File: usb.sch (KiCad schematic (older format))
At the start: 17 parts, among them J4 CONN_02X03, U1 LFE5U-85F-6BG381C, Y1 FNETHE025

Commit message: better RGB-OUT
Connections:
- net FTDI_RXD is gone; now on net LTDC_FROM_FPGA_G6: U1.L4 (PL56C)
- net LTDC_FROM_FPGA_B4 is gone; now on net LTDC_FROM_FPGA_G7: U1.L1 (PL65C)
- net LTDC_FROM_FPGA_R3 is gone; now on net LTDC_FROM_FPGA_R4: U1.G1 (PCLKC6_0)
- net OLED_CLK is gone; now on net LTDC_FROM_FPGA_B6: U1.P4 (GPLL0C_IN)
- net OLED_RES is gone; now on net LTDC_FROM_FPGA_B3: U1.P2 (PL92B)
- net WIFI_GPIO21 is gone; now on net LTDC_FROM_FPGA_G3: U1.K5 (VREF1_6)
- net LTDC_FROM_FPGA_B3: no longer U1.N3 (PL86A)
- net LTDC_FROM_FPGA_B6: no longer U1.N2 (PL65A)
- net LTDC_FROM_FPGA_DE: no longer U1.N5 (PL83B)
- net LTDC_FROM_FPGA_G3: no longer U1.H1 (PL53C)
- net LTDC_FROM_FPGA_G4: now also U1.K4 (PL56A); no longer U1.K2 (PL53A)
- net LTDC_FROM_FPGA_G6: no longer U1.K4 (PL56A)
- net LTDC_FROM_FPGA_G7: no longer U1.N4 (PL83C)
- net LTDC_FROM_FPGA_R4: no longer U1.J5 (PL50B)
- net LTDC_FROM_FPGA_R6: now also U1.H1 (PL53C); no longer U1.J1 (PL53B)
- net LTDC_FROM_FPGA_R7: now also U1.J5 (PL50B); no longer U1.K1 (PL53D)
- net FTDI_TXDEN renamed LTDC_FROM_FPGA_G2
- net LTDC_FROM_FPGA_B7 renamed OLED_DC
- net WIFI_RXD renamed LTDC_FROM_FPGA_G5
- new net OLED_CS: U1.N2 (PL65A)
- new net SD_CD: U1.N5 (PL83B)
- new net SD_CMD: U1.J1 (PL53B)
- new net SD_D2: U1.K1 (PL53D)
- new net SD_D3: U1.K2 (PL53A)
- new net WIFI_GPIO19: U1.N4 (PL83C)
- new net WIFI_GPIO27: U1.N3 (PL86A)
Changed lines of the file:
@@
 Text GLabel 10150 2650 2    60   Input ~ 0
 FTDI_TXD
-Text GLabel 8650 1950 0    60   Input ~ 0
-FTDI_RXD
 Text GLabel 10150 2450 2    60   Input ~ 0
 FTDI_nRTS
 Text GLabel 10150 2550 2    60   Input ~ 0
 FTDI_nDTR
-Text GLabel 8650 2050 0    60   Input ~ 0
-WIFI_TXD
-Text GLabel 10150 1550 2    60   Input ~ 0
-WIFI_RXD
 Text GLabel 10150 2350 2    60   Input ~ 0
 WIFI_GPIO0
 Text GLabel 10150 1450 2    60   Input ~ 0
 WIFI_EN
-Text GLabel 10150 2850 2    60   Input ~ 0
-OLED_RES
-Text GLabel 8650 2750 0    60   Input ~ 0
-OLED_MOSI
-Text GLabel 10150 2750 2    60   Input ~ 0
-OLED_CLK
 Text GLabel 8650 2850 0    60   Input ~ 0
 OLED_DC
@@
 Connection ~ 2600 2850
 Connection ~ 2700 2750
-Text GLabel 8650 2550 0    60   Input ~ 0
-WIFI_GPIO26
-Wire Wire Line
-	10150 1350 10750 1350
-Text Label 10200 1350 0    60   ~ 0
-ANT_433MHz
 Text Notes 650  4100 0    60   ~ 0
 D8,D9: Schottky 2A/30V \nLow drop Vfmax=0.375V\nParts reduction: Only D8 is required.\nD9 D51 D52 can be 1206\n1A polyfuses or 0-ohm/2A jumpers
@@
 Text Notes 2750 5350 0    60   ~ 0
 D- 1.5k pullp for \nlow speed device\nmode USB1.0
-Text GLabel 8650 2350 0    60   Input ~ 0
-FTDI_TXDEN
 $Comp
 L lfe5bg381:LFE5UM-85F-6BG381C U1
@@
 Text Label 1850 2650 0    60   ~ 0
 US2VBUS
-Text GLabel 8650 1750 0    60   Input ~ 0
-SD_D1
 Text Notes 750  6050 0    60   ~ 0
 Deviation from USB specification in\npulldowns for BOM simplificaton.\nWith series diode, correct value R63 R64 \nshould be 12k but 15k is used.
@@
 Text GLabel 10150 1950 2    60   Input ~ 0
 FTDI_nRXLED
-Text GLabel 10150 2050 2    60   Input ~ 0
-WIFI_GPIO21
-Text GLabel 10150 1650 2    60   Input ~ 0
-WIFI_GPIO22
 Text GLabel 8650 1650 0    60   Input ~ 0
 OLED_BL
-Text GLabel 7050 2450 0    60   Input ~ 0
+Text GLabel 10150 2850 2    60   Input ~ 0
 LTDC_FROM_FPGA_B3
-Text GLabel 7050 2550 0    60   Input ~ 0
-LTDC_FROM_FPGA_B4
-Text GLabel 7050 2650 0    60   Input ~ 0
+Text GLabel 10150 2750 2    60   Input ~ 0
 LTDC_FROM_FPGA_B6
-Text GLabel 11800 1750 2    60   Input ~ 0
-LTDC_FROM_FPGA_R7
-Text GLabel 11800 1650 2    60   Input ~ 0
+Text GLabel 10200 1350 2    60   Input ~ 0
 LTDC_FROM_FPGA_R4
-Text GLabel 11800 1950 2    60   Input ~ 0
-LTDC_FROM_FPGA_R5
-Text GLabel 11800 1850 2    60   Input ~ 0
+Text GLabel 8650 1750 0    60   Input ~ 0
 LTDC_FROM_FPGA_R6
-Text GLabel 7050 1650 0    60   Input ~ 0
+Text GLabel 6200 1650 0    60   Input ~ 0
 LTDC_FROM_FPGA_CLK
 Text GLabel 11800 2250 2    60   Input ~ 0
 LTDC_FROM_FPGA_DE
-Text GLabel 7050 2150 0    60   Input ~ 0
+Text GLabel 8650 2550 0    60   Input ~ 0
 LTDC_FROM_FPGA_G7
-Text GLabel 7050 2050 0    60   Input ~ 0
+Text GLabel 8650 1950 0    60   Input ~ 0
 LTDC_FROM_FPGA_G6
-Text GLabel 7050 1950 0    60   Input ~ 0
+Text GLabel 10150 1550 2    60   Input ~ 0
 LTDC_FROM_FPGA_G5
-Text GLabel 7050 1850 0    60   Input ~ 0
+Text GLabel 10150 2050 2    60   Input ~ 0
+LTDC_FROM_FPGA_G3
+Text GLabel 8650 2350 0    60   Input ~ 0
+LTDC_FROM_FPGA_G2
+Text GLabel 6300 1650 2    60   Input ~ 0
+OLED_BL
+Wire Wire Line
+	6200 1650 6300 1650
+Text GLabel 8650 2750 0    60   Input ~ 0
+LTDC_FROM_FPGA_B5
+Wire Wire Line
+	10150 1350 10200 1350
+Text GLabel 8650 2050 0    60   Input ~ 0
 LTDC_FROM_FPGA_G4
-Text GLabel 7050 1750 0    60   Input ~ 0
-LTDC_FROM_FPGA_G3
-Text GLabel 7050 2350 0    60   Input ~ 0
-LTDC_FROM_FPGA_G2
-Text GLabel 7150 1650 2    60   Input ~ 0
-OLED_BL
-Text GLabel 7150 1750 2    60   Input ~ 0
-SD_D1
-Text GLabel 7150 1850 2    60   Input ~ 0
-SD_D3
-Text GLabel 7150 1950 2    60   Input ~ 0
-FTDI_RXD
-Text GLabel 7150 2050 2    60   Input ~ 0
-WIFI_TXD
-Text GLabel 7150 2150 2    60   Input ~ 0
-WIFI_GPIO19
-Text GLabel 7150 2350 2    60   Input ~ 0
-FTDI_TXDEN
-Text GLabel 7150 2450 2    60   Input ~ 0
-WIFI_GPIO27
-Text GLabel 7150 2550 2    60   Input ~ 0
-WIFI_GPIO26
-Text GLabel 7150 2650 2    60   Input ~ 0
-OLED_CS
-Text GLabel 7150 2750 2    60   Input ~ 0
-OLED_MOSI
-Text GLabel 7150 2850 2    60   Input ~ 0
-OLED_DC
-Wire Wire Line
-	7050 1650 7150 1650
-Wire Wire Line
-	7050 1750 7150 1750
-Wire Wire Line
-	7050 1850 7150 1850
-Wire Wire Line
-	7050 1950 7150 1950
-Wire Wire Line
-	7050 2050 7150 2050
-Wire Wire Line
-	7050 2150 7150 2150
-Wire Wire Line
-	7050 2350 7150 2350
-Wire Wire Line
-	7050 2450 7150 2450
-Wire Wire Line
-	7150 2550 7050 2550
-Wire Wire Line
-	7050 2650 7150 2650
-Wire Wire Line
-	7050 2750 7150 2750
-Wire Wire Line
-	7150 2850 7050 2850
-Text GLabel 11700 1650 0    60   Input ~ 0
-WIFI_GPIO22
-Text GLabel 11700 1750 0    60   Input ~ 0
-SD_D2
-Text GLabel 11700 1850 0    60   Input ~ 0
-SD_CMD
-Text GLabel 11700 1950 0    60   Input ~ 0
-FTDI_nRXLED
-Text GLabel 11700 2250 0    60   Input ~ 0
-SD_CD
-Wire Wire Line
-	11800 1650 11700 1650
-Wire Wire Line
-	11700 1750 11800 1750
-Wire Wire Line
-	11800 1850 11700 1850
-Wire Wire Line
-	11700 1950 11800 1950
-Wire Wire Line
-	11700 2250 11800 2250
-Text GLabel 10750 1350 2    60   Input ~ 0
-LTDC_FROM_FPGA_R3
-Text GLabel 7050 2750 0    60   Input ~ 0
-LTDC_FROM_FPGA_B5
-Text GLabel 7050 2850 0    60   Input ~ 0
-LTDC_FROM_FPGA_B7
+Text GLabel 10150 1650 2    60   Input ~ 0
+LTDC_FROM_FPGA_R7
 $EndSCHEMATC

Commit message: More fixes
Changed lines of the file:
@@
 Text GLabel 10150 1950 2    60   Input ~ 0
 FTDI_nRXLED
-Text GLabel 8650 1650 0    60   Input ~ 0
-OLED_BL
 Text GLabel 10150 2850 2    60   Input ~ 0
 LTDC_FROM_FPGA_B3
@@
 Text GLabel 8650 1750 0    60   Input ~ 0
 LTDC_FROM_FPGA_R6
-Text GLabel 6200 1650 0    60   Input ~ 0
+Text GLabel 8650 1650 0    60   Input ~ 0
 LTDC_FROM_FPGA_CLK
 Text GLabel 11800 2250 2    60   Input ~ 0
@@
 Text GLabel 8650 2350 0    60   Input ~ 0
 LTDC_FROM_FPGA_G2
-Text GLabel 6300 1650 2    60   Input ~ 0
-OLED_BL
-Wire Wire Line
-	6200 1650 6300 1650
 Text GLabel 8650 2750 0    60   Input ~ 0
 LTDC_FROM_FPGA_B5

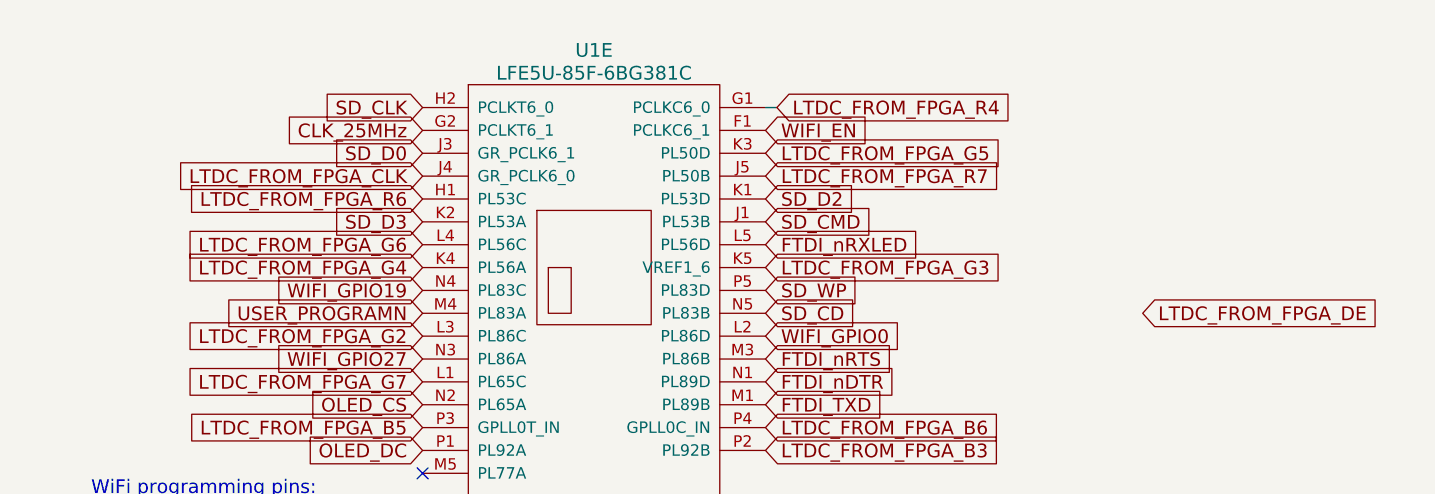
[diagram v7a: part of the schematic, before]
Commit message: Adding all SPI to FPGA resorting LCD TO FPGA
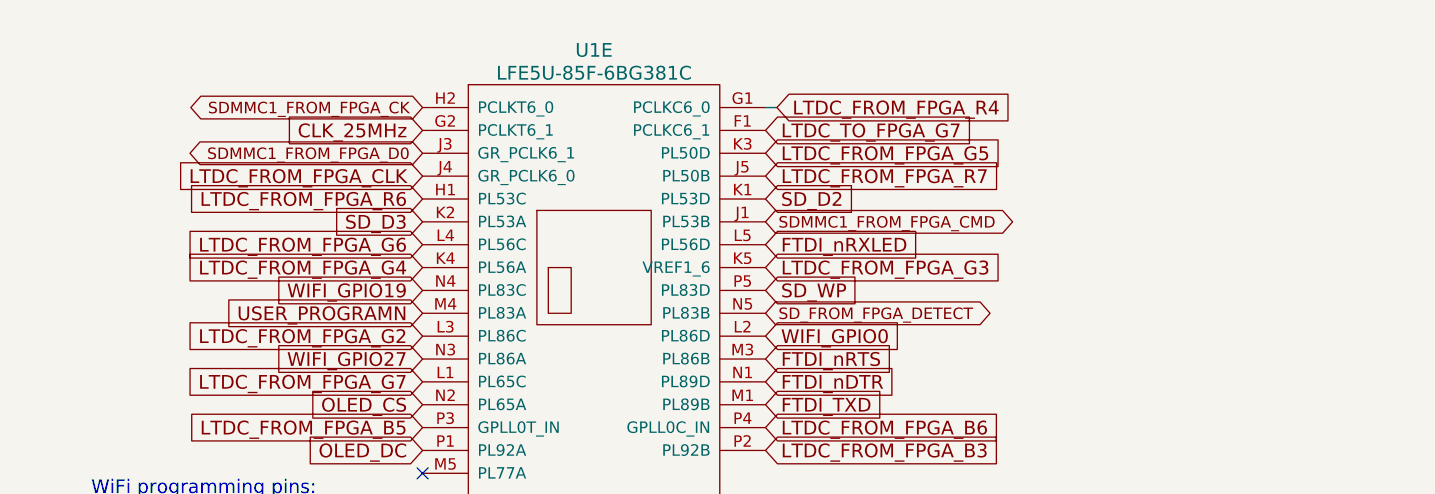
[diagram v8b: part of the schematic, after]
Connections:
- net SD_CD renamed SD_FROM_FPGA_DETECT
- net SD_CLK renamed SDMMC1_FROM_FPGA_CK
- net SD_CMD renamed SDMMC1_FROM_FPGA_CMD
- net SD_D0 renamed SDMMC1_FROM_FPGA_D0
- net WIFI_EN renamed LTDC_TO_FPGA_G7
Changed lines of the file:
@@
 Text GLabel 10150 2350 2    60   Input ~ 0
 WIFI_GPIO0
-Text GLabel 10150 1450 2    60   Input ~ 0
-WIFI_EN
 Text GLabel 8650 2850 0    60   Input ~ 0
 OLED_DC
 Text GLabel 8650 2650 0    60   Input ~ 0
 OLED_CS
-Text GLabel 8650 1550 0    60   Input ~ 0
-SD_D0
 Text GLabel 10150 1750 2    60   Input ~ 0
 SD_D2
 Text GLabel 8650 1850 0    60   Input ~ 0
 SD_D3
-Text GLabel 8650 1350 0    60   Input ~ 0
-SD_CLK
-Text GLabel 10150 1850 2    60   Input ~ 0
-SD_CMD
 Text GLabel 10150 2150 2    60   Input ~ 0
 SD_WP
-Text GLabel 10150 2250 2    60   Input ~ 0
-SD_CD
 Text Notes 7200 3150 0    60   ~ 0
 WiFi programming pins:\nTXD RXD RTS DTR
@@
 Text GLabel 8650 1650 0    60   Input ~ 0
 LTDC_FROM_FPGA_CLK
-Text GLabel 11800 2250 2    60   Input ~ 0
-LTDC_FROM_FPGA_DE
 Text GLabel 8650 2550 0    60   Input ~ 0
 LTDC_FROM_FPGA_G7
@@
 Text GLabel 10150 1650 2    60   Input ~ 0
 LTDC_FROM_FPGA_R7
+Text GLabel 10150 2250 2    50   BiDi ~ 0
+SD_FROM_FPGA_DETECT
+Text GLabel 10150 1850 2    50   BiDi ~ 0
+SDMMC1_FROM_FPGA_CMD
+Text GLabel 8650 1550 0    50   BiDi ~ 0
+SDMMC1_FROM_FPGA_D0
+Text GLabel 8650 1350 0    50   BiDi ~ 0
+SDMMC1_FROM_FPGA_CK
+Text GLabel 10150 1450 2    60   Input ~ 0
+LTDC_TO_FPGA_G7
 $EndSCHEMATC
